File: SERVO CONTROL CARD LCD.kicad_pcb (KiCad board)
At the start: 2 copper layers, 112 x 56 mm, 62 parts, among them J1 Conn_01x02, J2 Conn_01x02, J3 Conn_01x05, J4 Conn_01x02, J5 Conn_01x02, J6 Conn_01x03, K1 FINDER-34.51, Q1 BT136-500, Q2 BT136-500, Q3 BC547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

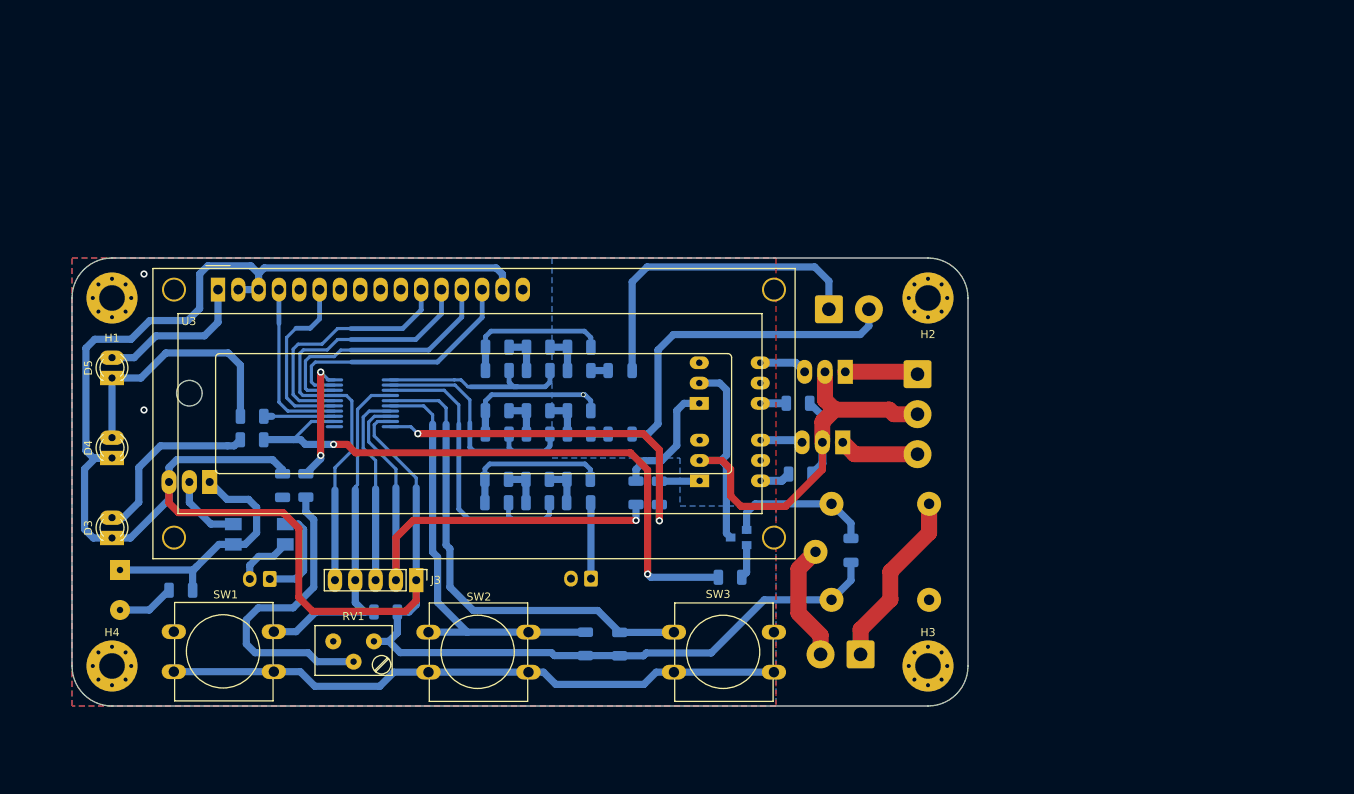
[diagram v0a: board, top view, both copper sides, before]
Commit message: pcb board hase standard size
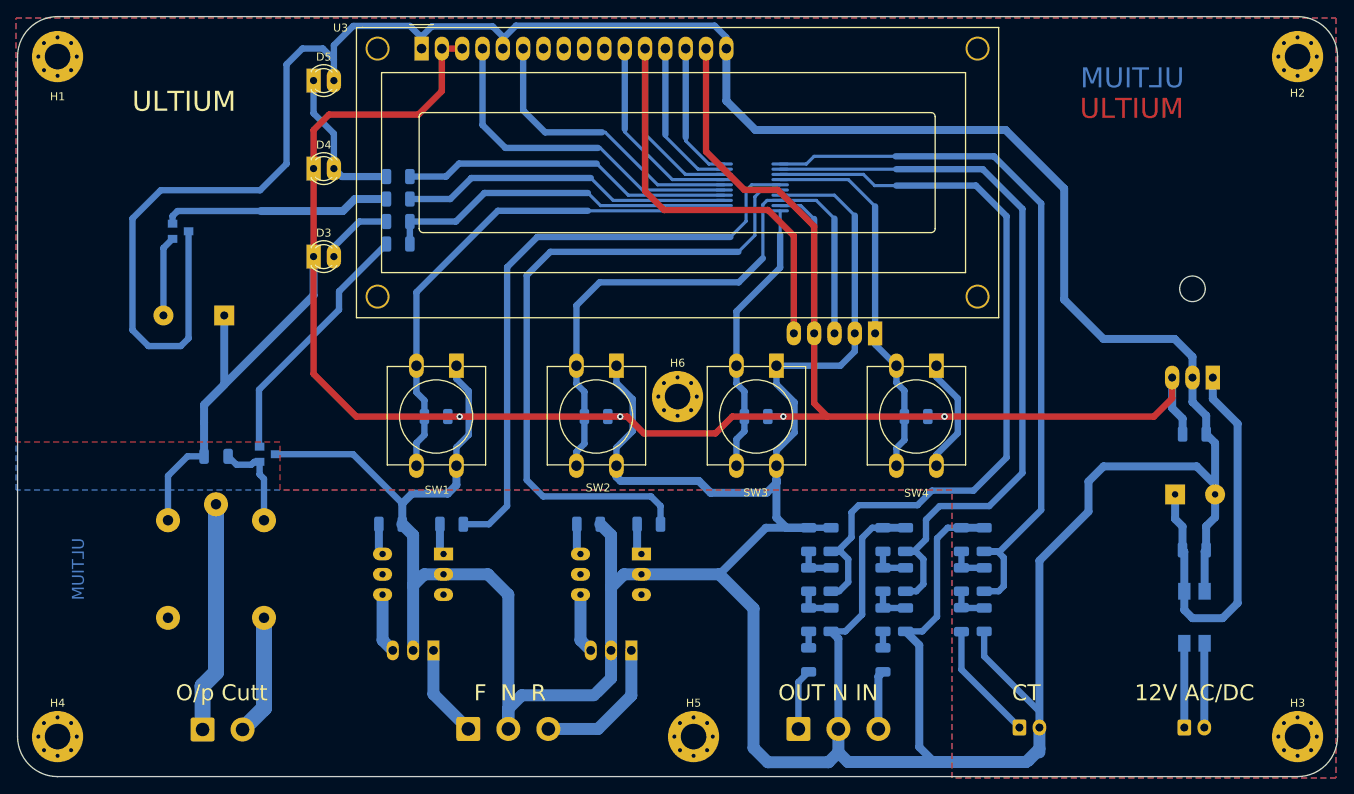
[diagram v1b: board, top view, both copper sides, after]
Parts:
- removed R16: 10K, My Custom Footprint:R_1206_3216Metric
- removed RV1: R_POT, My Custom Footprint:Potentiometer_Trimmer_Bourns_3299Y
- added BZ1: Buzzer, Buzzer_Beeper:Buzzer_12x9.5RM7.6, B.Cu at (96.9, 80.9)
- added H5: MountingHole, MountingHole:MountingHole_3.2mm_M3_Pad_Via, F.Cu at (155.5, 133.5)
- added H6: MountingHole, MountingHole:MountingHole_3.2mm_M3_Pad_Via, F.Cu at (153.5, 91.0)
- added Q4: BC547, My Custom Footprint:SOT-23_Transistor, B.Cu at (91.4, 70.3)
- added R23: 10K, My Custom Footprint:R_1206_3216Metric, B.Cu at (183.3, 93.5)
- added R24: 10K, My Custom Footprint:R_1206_3216Metric, B.Cu at (118.6, 66.3)
- added SW4: SW_DIP_x01, Button_Switch_THT:SW_PUSH-12mm, F.Cu at (185.9, 87.1)
- J3: moved to B.Cu
- J5: value Conn_01x02 -> Conn_01x03; footprint Connector_JST:JST_NV_B02P-NV_1x02_P5.00mm_Vertical -> Connector_JST:JST_NV_B03P-NV_1x03_P5.00mm_Vertical
- moved C4 132.2 mm to (215.7, 103.2), turned to 0 degrees
- moved C3 126.8 mm to (218.1, 110.2), turned to 180 degrees
- moved U2 126.1 mm to (220.4, 88.6)
- moved D7 117.4 mm to (218.1, 118.6), turned to 270 degrees
- moved J1 115.8 mm to (216.9, 132.4), turned to 0 degrees
- moved C7 114.2 mm to (218.1, 95.7), turned to 180 degrees
- moved J2 82.8 mm to (94.1, 132.6), turned to 0 degrees
- moved D8 80.2 mm to (95.8, 98.5), turned to 0 degrees
- moved K1 75.2 mm to (95.8, 104.5), turned to 270 degrees
- moved J6 71.6 mm to (127.4, 132.5), turned to 0 degrees
- moved J3 65.1 mm to (178.2, 83.1), turned to 90 degrees
- moved Q1 62.2 mm to (123.0, 122.7)
- moved C10 61.1 mm to (191.8, 108.9), turned to 90 degrees
- moved Q3 59.8 mm to (102.3, 98.2), turned to 0 degrees
- moved R14 58.8 mm to (118.6, 71.9), turned to 0 degrees
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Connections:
- J1 pad 1: Net-(D7-Pad4) -> Net-(D7-Pad3)
- J1 pad 2: Net-(D7-Pad3) -> Net-(D7-Pad4)
- J3 pad 1: VDD -> SW_4
- J3 pad 2: Reverse_Controlling -> VSS
- J3 pad 3: VSS -> SW_2
- J3 pad 4: SW_1 -> VDD
- J5 pad 2: INPUT_volt -> VSS
- K1 pad 11: Net-(J2-Pad2) -> Net-(J2-Pad1)
- K1 pad 12: Net-(K1-Pad12) -> (no net)
- K1 pad 14: Net-(J2-Pad1) -> Net-(J2-Pad2)
- U1 pad 1: O-P_voltage -> Current
- U1 pad 10: Forward_controlling -> SW_3
- U1 pad 11: Net-(U1-Pad11) -> SW_1
- U1 pad 13: Auto_led -> Buzzer
- U1 pad 14: RS -> Auto_led
- U1 pad 15: E -> RS
- U1 pad 16: DB4 -> E
- U1 pad 17: DB5 -> DB4
- U1 pad 18: DB6 -> DB5
- U1 pad 19: DB7 -> DB6
- U1 pad 20: POT -> DB7
- U1 pad 3: Current -> O-P_voltage
- U1 pad 4: SW_1 -> SW_4
- U1 pad 5: SW_3 -> Reverse_Controlling
- U1 pad 6: SW_2 -> Forward_controlling
- U1 pad 8: Reverse_Controlling -> SW_2
- U3 pad 10: Net-(U3-Pad10) -> (no net)
- U3 pad 7: Net-(U3-Pad7) -> (no net)
- U3 pad 8: Net-(U3-Pad8) -> (no net)
- U3 pad 9: Net-(U3-Pad9) -> (no net)
- U4 pad 3: Net-(U4-Pad3) -> (no net)
- U4 pad 5: Net-(U4-Pad5) -> (no net)
- U5 pad 3: Net-(U5-Pad3) -> (no net)
- U5 pad 5: Net-(U5-Pad5) -> (no net)
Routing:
- net VSS: track 276.9 -> 816.8 mm, vias 3 -> 0
- net O-P_voltage: track 24.7 -> 97.3 mm
- net I-P_voltage: track 30.9 -> 93.8 mm
- net Current: track 38.1 -> 92.1 mm
- net SW_4: track 0.00 -> 52.4 mm
- net Buzzer: track 0.00 -> 41.5 mm
- net Forward_controlling: track 45.7 -> 84.9 mm, vias 2 -> 0
- net Net-(R16-Pad2): track 39.1 -> 0.00 mm
- net VDD: track 276.5 -> 312.3 mm, vias 0 -> 4
- net INPUT_volt: track 42.7 -> 7.38 mm
- net Output_Relay: track 77.7 -> 44.2 mm, vias 2 -> 0
- net RS: track 21.5 -> 54.7 mm
- net OUTPUT_volt: track 40.7 -> 7.67 mm
- net Auto_led: track 8.82 -> 41.6 mm
- net SW_1: track 44.3 -> 76.5 mm
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- added copper zone on F.Cu, net VDD
- removed copper zone on F.Cu, net VSS
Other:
- board size 112 x 56 mm -> 165 x 95 mm
- board text added: "12V AC/DC"
- board text added: "CT"
- board text added: "F N R"
- board text added: "IN N OUT"
- board text added: "O/p Cutt"
- board text added: "OUT N IN"
- board text added: "R N F"
- board text added: "ULTIUM"

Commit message: pcb board hase standard size with block connector v1.2
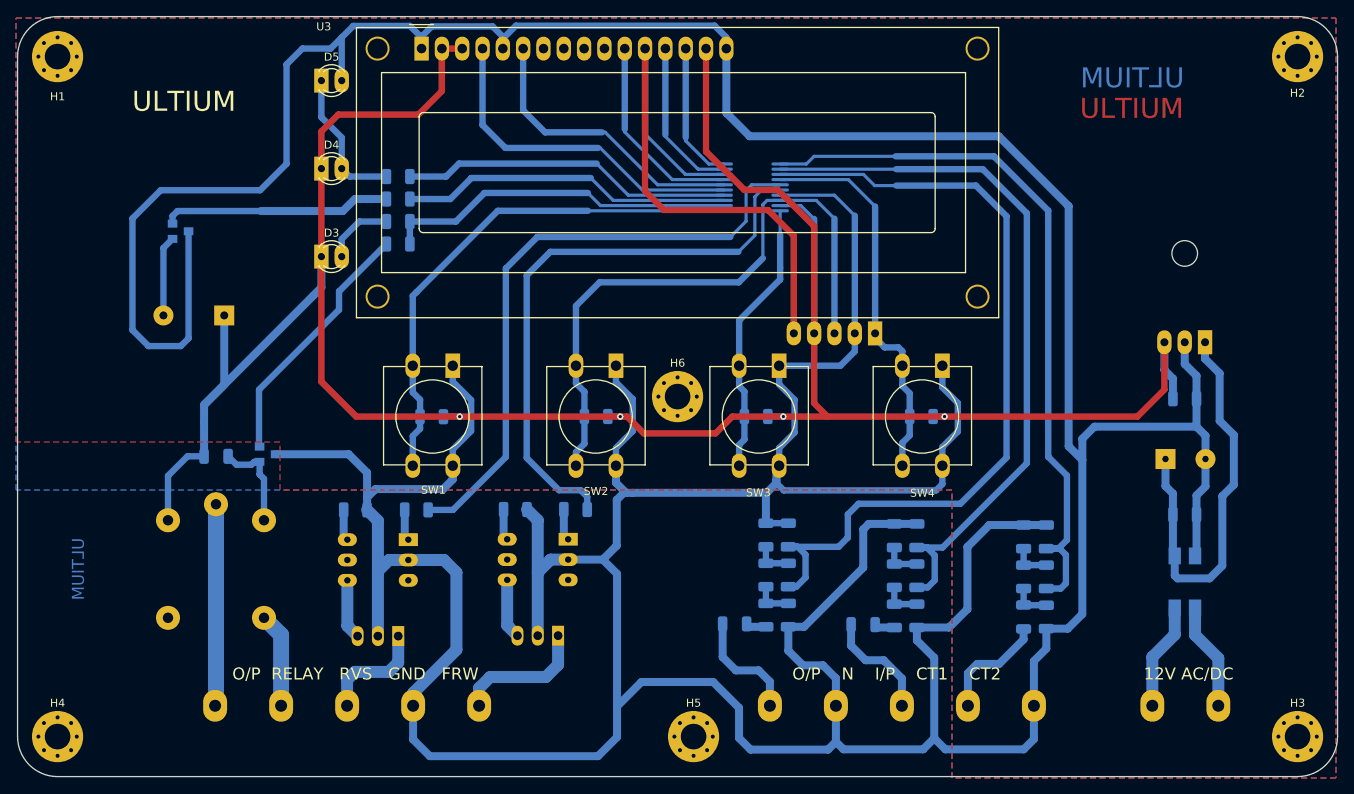
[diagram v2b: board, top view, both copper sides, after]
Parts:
- removed J5, J6: Conn_01x03, Connector_JST:JST_NV_B03P-NV_1x03_P5.00mm_Vertical
- J1: footprint Connector_JST:JST_EH_B2B-EH-A_1x02_P2.50mm_Vertical -> My Custom Footprint:Block_connector_2x1_H1.5_P8
- J2: value Conn_01x02 -> Conn_01x05; footprint Connector_JST:JST_NV_B02P-NV_1x02_P5.00mm_Vertical -> My Custom Footprint:Block_connector_5x1_H1.5_P8
- J4: value Conn_01x02 -> Conn_01x05; footprint Connector_JST:JST_EH_B2B-EH-A_1x02_P2.50mm_Vertical -> My Custom Footprint:Block_connector_5x1_H1.5_P8
- moved J2 104.0 mm to (198.1, 129.6), turned to 180 degrees
- moved J4 67.6 mm to (128.7, 129.6), turned to 180 degrees
- moved D1 10.3 mm to (160.7, 119.4), turned to 180 degrees
- moved R12 9.34 mm to (133.2, 105.1)
- moved R8 9.34 mm to (140.8, 105.1)
- moved U5 9.34 mm to (139.8, 108.8)
- moved Q2 9.34 mm to (138.6, 120.9)
- moved C10 7.78 mm to (199.6, 108.5)
- moved C9 7.78 mm to (196.8, 108.5)
- moved D9 7.78 mm to (196.8, 118.5)
- moved R20 7.78 mm to (199.6, 118.5)
- moved R21 7.78 mm to (196.8, 113.5)
- moved R22 7.78 mm to (199.6, 113.5)
- moved C1 5.37 mm to (164.6, 108.3)
- moved C2 5.37 mm to (167.4, 108.3)
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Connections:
- D9 pad 2: Net-(D9-Pad2) -> CT_input
- J1 pad 1: Net-(D7-Pad3) -> Net-(D7-Pad4)
- J1 pad 2: Net-(D7-Pad4) -> Net-(D7-Pad3)
- J2 pad 1: Net-(J2-Pad1) -> VSS
- J2 pad 2: Net-(J2-Pad2) -> CT_input
- J4 pad 1: Net-(D9-Pad2) -> Forward
- K1 pad 11: Net-(J2-Pad1) -> Op_cutt1
- K1 pad 12: (no net) -> Net-(K1-Pad12)
- K1 pad 14: Net-(J2-Pad2) -> Op_cutt2
- U3 pad 10: (no net) -> Net-(U3-Pad10)
- U3 pad 7: (no net) -> Net-(U3-Pad7)
- U3 pad 8: (no net) -> Net-(U3-Pad8)
- U3 pad 9: (no net) -> Net-(U3-Pad9)
- U4 pad 3: (no net) -> Net-(U4-Pad3)
- U4 pad 5: (no net) -> Net-(U4-Pad5)
- U5 pad 3: (no net) -> Net-(U5-Pad3)
- U5 pad 5: (no net) -> Net-(U5-Pad5)
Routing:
- net Net-(J2-Pad1): track 28.9 -> 0.00 mm
- net Op_cutt1: track 0.00 -> 25.4 mm
- net Net-(J2-Pad2): track 15.1 -> 0.00 mm
- net Net-(D9-Pad2): track 15.0 -> 0.00 mm
- net CT_input: track 0.00 -> 14.1 mm
- net Forward_controlling: track 84.9 -> 72.9 mm
- net Op_cutt2: track 0.00 -> 11.9 mm
- net INPUT_volt: track 7.38 -> 14.1 mm
- net OUTPUT_volt: track 7.67 -> 14.3 mm
- net O-P_voltage: track 97.3 -> 103.1 mm
- net SW_4: track 52.4 -> 48.9 mm
- net I-P_voltage: track 93.8 -> 90.6 mm
- net VDD: track 312.3 -> 315.3 mm
- net Net-(D7-Pad4): track 10.5 -> 13.5 mm
- net Net-(D7-Pad3): track 10.5 -> 13.4 mm
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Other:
- board text added: "CT1 CT2 I/P N O/P"
- board text added: "FRW GND RVS O/P RELAY"
- board text added: "O/P N I/P CT1 CT2"
- board text added: "O/P RELAY RVS GND FRW"
- board text removed: "CT"
- board text removed: "F N R"
- board text removed: "IN N OUT"
- board text removed: "O/p Cutt"
- board text removed: "OUT N IN"
- board text removed: "R N F"
